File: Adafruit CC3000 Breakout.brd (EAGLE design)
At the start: 39.4 x 59.7 mm, 33 parts, among them IC1 ATmega1284P, U1 CC3000MOD, X1 2500AT44M0400E

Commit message: Route.
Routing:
- net VBAT: track 20.6 -> 103.8 mm, vias 0 -> 1
- net N$18: track 0.00 -> 40.9 mm
- net N$13: track 0.00 -> 38.9 mm, vias 0 -> 2
- net VBAT_EN_3V: track 0.00 -> 38.0 mm, vias 0 -> 2
- net RESET: track 0.00 -> 35.8 mm, vias 0 -> 2
- net VIN: track 0.00 -> 34.6 mm, vias 0 -> 1
- net N$14: track 0.00 -> 33.6 mm, vias 0 -> 1
- net SPI_CLK_3V: track 0.00 -> 27.4 mm, vias 0 -> 2
- net SPI_MISO_3V: track 0.00 -> 24.7 mm, vias 0 -> 1
- net SPI_MOSI_3V: track 0.00 -> 23.6 mm, vias 0 -> 3
- net N$15: track 0.00 -> 23.5 mm
- net N$16: track 0.00 -> 23.2 mm
- net SPI_CS_3V: track 0.00 -> 22.8 mm, vias 0 -> 2
- net N$5: track 0.00 -> 18.3 mm
- net N$9: track 0.00 -> 17.6 mm
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
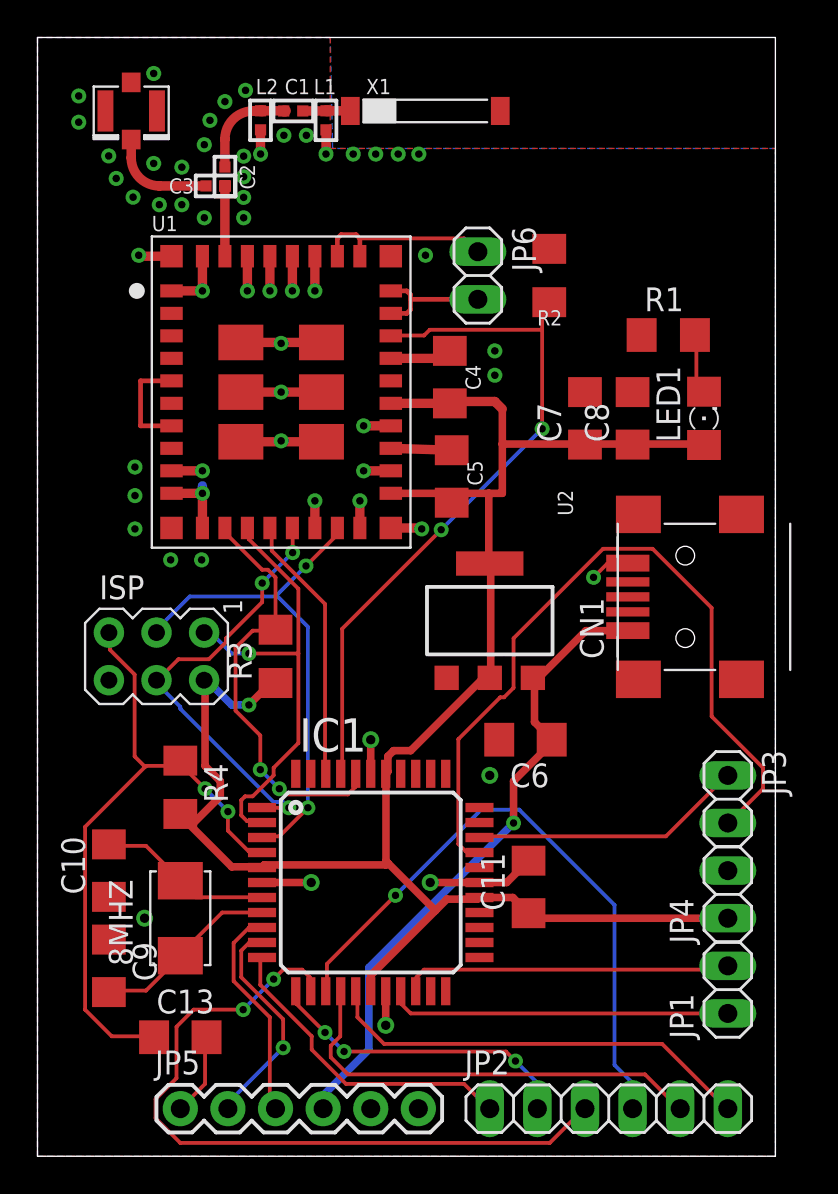
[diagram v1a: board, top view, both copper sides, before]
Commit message: Silk screen (and name some traces).
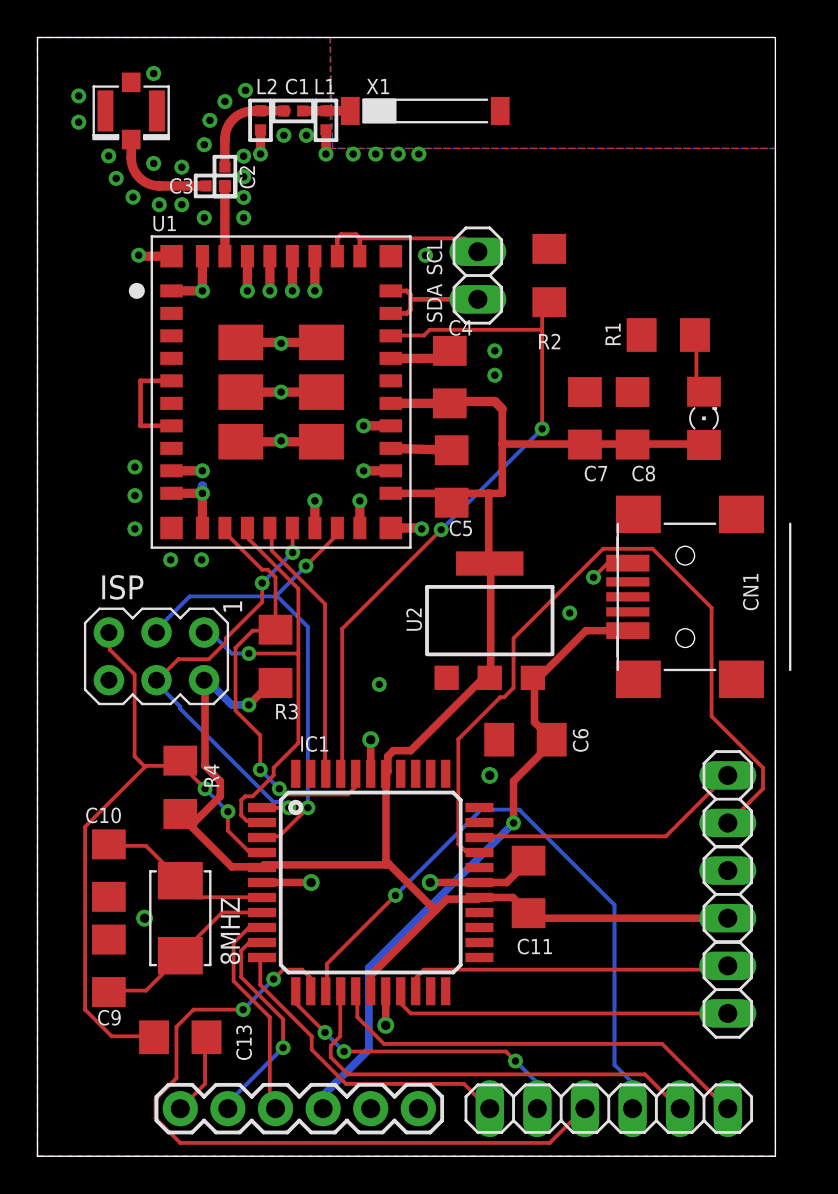
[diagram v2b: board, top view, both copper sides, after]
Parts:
- LED1: value green -> Power
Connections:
- net N$11 renamed RX1
- net N$12 renamed TX1
- net N$13 renamed PD4
- net N$14 renamed PD5
- net N$15 renamed PD6
- net N$16 renamed PD7
- net N$17 renamed PA6
- net N$18 renamed PA7
- net N$5 renamed SCL
- net N$9 renamed SDA
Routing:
- net GND: track 62.7 -> 62.3 mm, vias 58 -> 60
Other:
- board text added: "B"
- board text added: "G"
- board text added: "GND"
- board text added: "PA6"
- board text added: "PA7"
- board text added: "PD4"
- board text added: "PD5"
- board text added: "PD6"
- board text added: "PD7"
- board text added: "RX1"
- board text added: "SCL"
- board text added: "SDA"
- board text added: "TX1"
- board text added: "VCC"
